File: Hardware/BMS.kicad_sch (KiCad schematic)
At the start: 16 parts, among them IC1 STM32H742VIT6

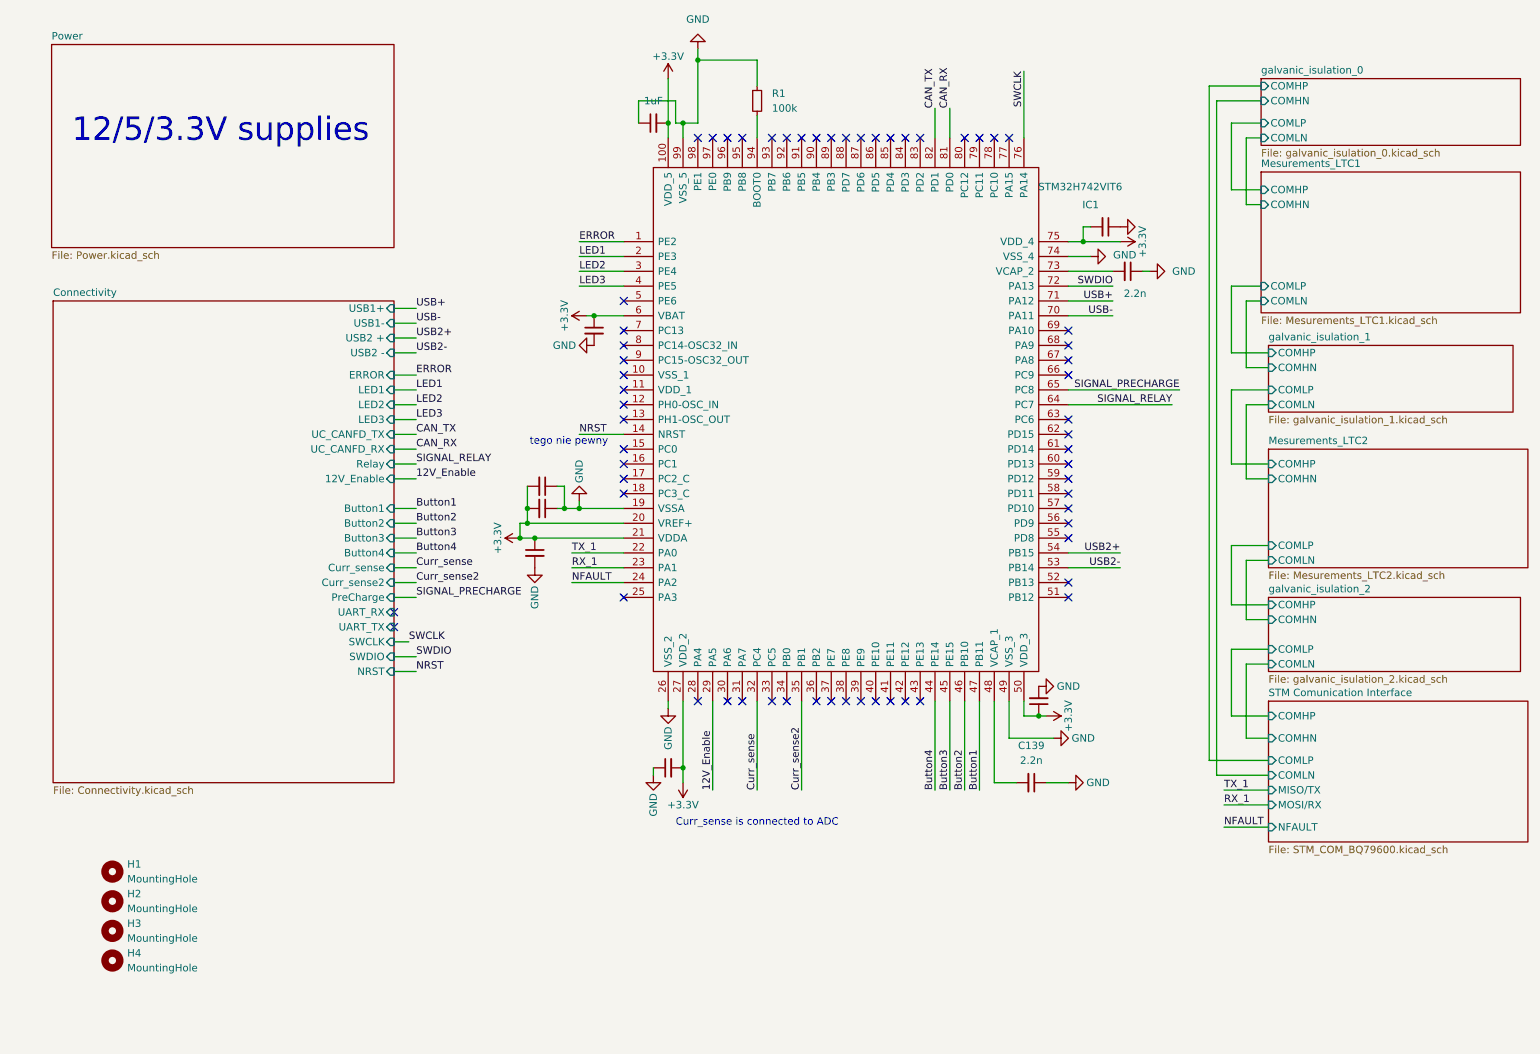
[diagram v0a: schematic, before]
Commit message: Bms plug and play, 2nd iteration with the same pinout
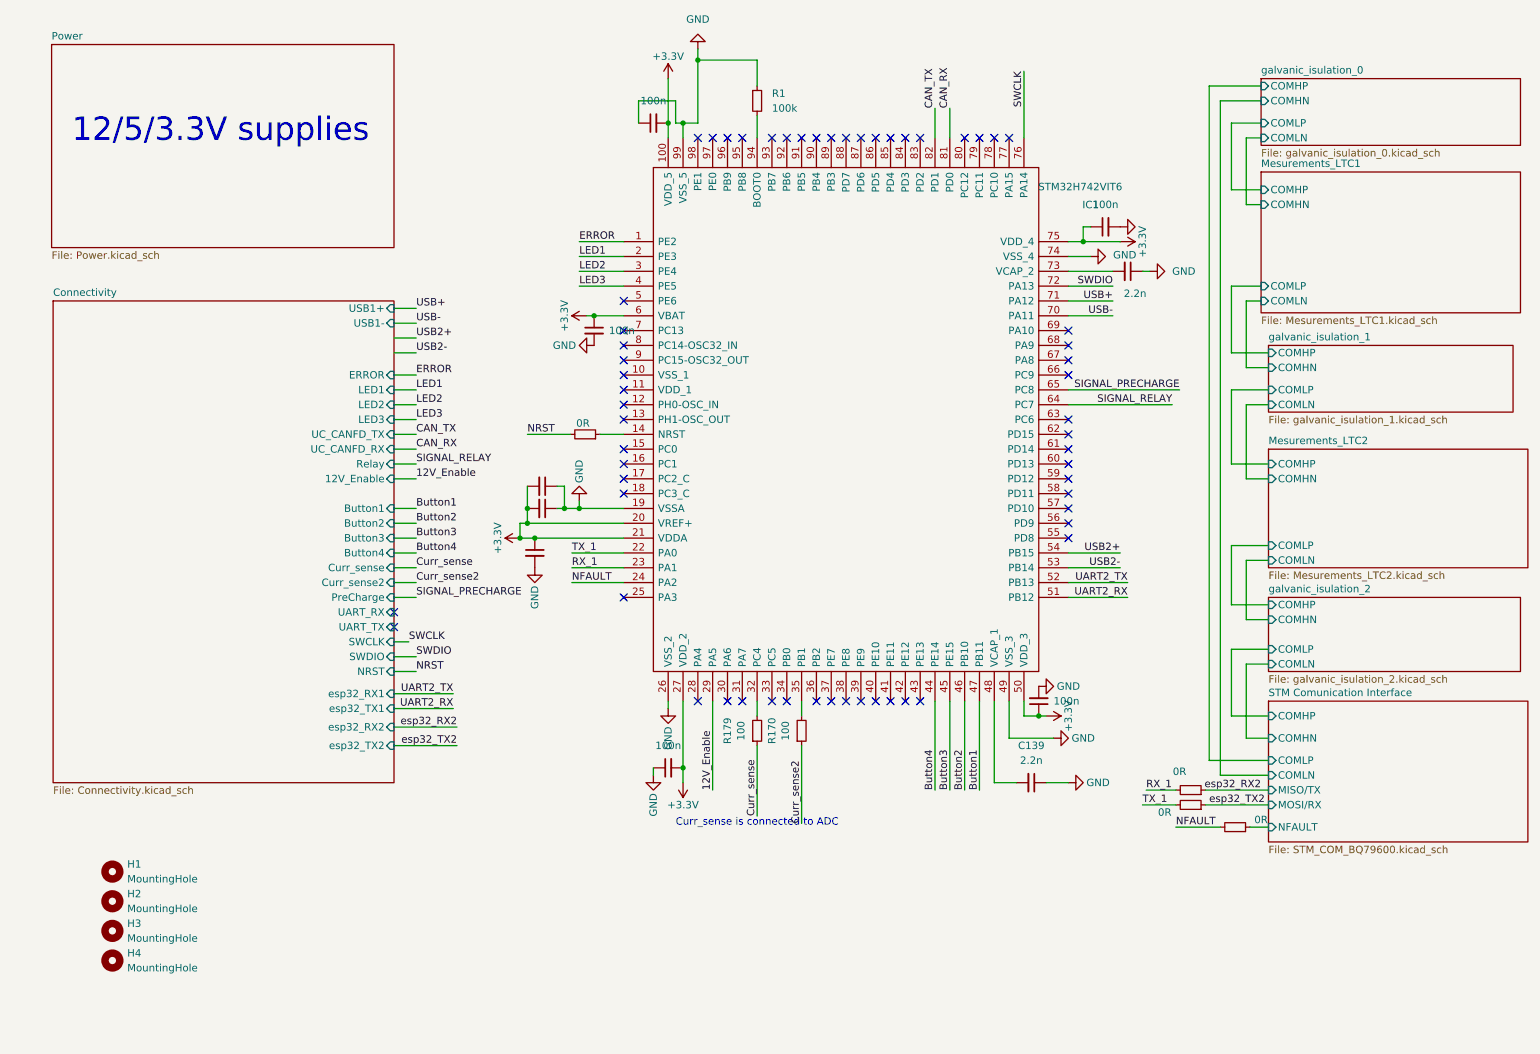
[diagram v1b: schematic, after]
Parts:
- added R170, R179: 100, Resistor_SMD:R_0603_1608Metric_Pad0.98x0.95mm_HandSolder, symbol Device:R_Small
- added R91, R92, R93, R94: 0R, Resistor_SMD:R_0603_1608Metric, symbol Device:R_Small
- C65, C67, C68, C69, C70: value 1uF -> 100n
- IC1: Description_1 (none) -> ARM Microcontrollers - MCU 16/32-BITS MICROS
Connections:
- net +3.3V: now also C69.1; no longer C69.2
- net Curr_sense: now also R179.1; no longer IC1.32 (PC4)
- net Curr_sense2: now also R170.1; no longer IC1.35 (PB1)
- net GND: now also C140.1, C69.2; no longer C69.1
- net NFAULT: now also R93.2
- net NRST: now also R94.2; no longer IC1.14 (NRST)
- net RX_1: now also R91.2
- net TX_1: now also R92.2
- net UART2_RX: now reaches IC1.51 (PB12)
- net UART2_TX: now reaches IC1.52 (PB13)
- new net: IC1.35 (PB1), R170.2
- new net: IC1.14 (NRST), R94.1
- new net: IC1.32 (PC4), R179.2
- new net STM Comunication Interface/NFAULT: R93.1
- new net esp32_RX2: R91.1
- new net esp32_TX2: R92.1
- no-connect marks 62 -> 60
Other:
- sheet STM Comunication Interface  renamed STM Comunication Interface
- sheet Connectivity ports: added esp32_RX1, esp32_RX2, esp32_TX1, esp32_TX2; removed USB2 +, USB2 -
- note removed: "tego nie pewny"

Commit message: nearly done
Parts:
- added R127, R128: 0R, Resistor_SMD:R_0603_1608Metric, symbol Device:R_Small
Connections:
- net esp32_RX2: now also R127.2; no longer R91.1
- net esp32_TX2: now also R128.2; no longer R92.1
- net SPI_MISO: now reaches IC1.30 (PA6)
- net SPI_MOSI: now reaches IC1.31 (PA7)
- net SIGNAL_RELAY2: now reaches IC1.63 (PC6)
- net SPI_CLK: now reaches IC1.89 (PB3)
- new net STM Comunication Interface/MISO/TX: R127.1, R91.1
- new net STM Comunication Interface/MOSI/RX: R128.1, R92.1
- no-connect marks 60 -> 56
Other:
- sheet Connectivity ports: added SPI_CLK, SPI_MISO, SPI_MOSI, relay_enable3; removed none

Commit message: New connectors jst_xh for low voltage side of bms
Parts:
- removed R170, R179: 100, Resistor_SMD:R_0603_1608Metric_Pad0.98x0.95mm_HandSolder, symbol Device:R_Small
- added F53, F54: 01550900M, footrpint:01550900M, symbol Device:Fuse_Small
- added J1: Conn_01x02, Connector_JST:JST_XH_S2B-XH-A_1x02_P2.50mm_Horizontal, symbol Connector_Generic:Conn_01x02
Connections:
- net SPI_MISO: now also IC1.90 (PB4); no longer IC1.30 (PA6)
- net Analog_Input2: now reaches IC1.32 (PC4)
- net Analog_Input3: now reaches IC1.33 (PC5)
- net Analog_Input4: now reaches IC1.34 (PB0)
- new net: F54.2, J1.2 (Pin_2)
- new net: F53.2, J1.1 (Pin_1)
- new net Analog_Input1: IC1.30 (PA6)
- new net Stack+: F53.1
- new net Stack-: F54.1
- no-connect marks 56 -> 54
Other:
- sheet Connectivity ports: added Analog_Input1, Analog_Input2, Analog_Input3, Analog_Input4; removed Curr_sense, Curr_sense2
- title: (none) -> Battery Management System for a high power gokart battery
- moved on the sheet: H1, H2, H3, H4

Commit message: Ready to review
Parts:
- H1, H2, H3, H4: now in the parts list
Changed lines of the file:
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@@
 		(body_style 1)
 		(exclude_from_sim no)
-		(in_bom no)
+		(in_bom yes)
 		(on_board yes)
 		(in_pos_files yes)
@@
 		(body_style 1)
 		(exclude_from_sim no)
-		(in_bom no)
+		(in_bom yes)
 		(on_board yes)
 		(in_pos_files yes)
@@
 		(body_style 1)
 		(exclude_from_sim no)
-		(in_bom no)
+		(in_bom yes)
 		(on_board yes)
 		(in_pos_files yes)
@@
 		(body_style 1)
 		(exclude_from_sim no)
-		(in_bom no)
+		(in_bom yes)
 		(on_board yes)
 		(in_pos_files yes)
